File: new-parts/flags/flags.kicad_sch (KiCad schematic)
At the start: 12 parts, among them J1 BHR-10-VUA, J2 Conn_02x03_Odd_Even, K1 J104D2C12VDC.15S

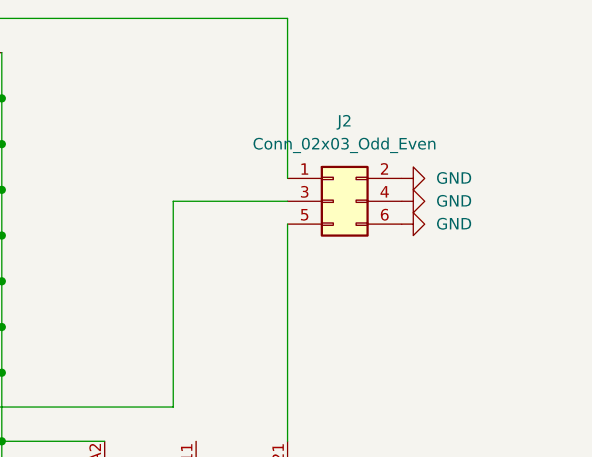
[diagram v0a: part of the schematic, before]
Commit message: Change all two-pin headers for control + ground to control only.
This is to prevent accidental short circuits when they are plugged in the
wrong way.
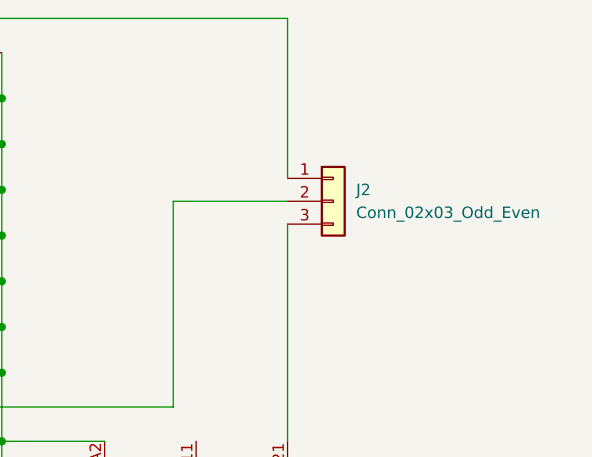
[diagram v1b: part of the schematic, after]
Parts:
- J2: footprint Connector_IDC:IDC-Header_2x03_P2.54mm_Vertical -> Connector_PinHeader_2.54mm:PinHeader_1x03_P2.54mm_Vertical; symbol Connector_Generic:Conn_02x03_Odd_Even -> Connector_Generic:Conn_01x03
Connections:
- net GND: no longer J2.2 (Pin_2), J2.4 (Pin_4), J2.6 (Pin_6)
- net at D8.2 (A), J1.8 (Pin_8): now also J2.2 (Pin_2); no longer J2.3 (Pin_3)
- net at K1.21: now also J2.3 (Pin_3); no longer J2.5 (Pin_5)
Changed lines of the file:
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@@
-    )
-  )
-  (symbol (lib_id "power:GND") (at 137.16 80.01 90) (unit 1)
-    (in_bom yes) (on_board yes) (dnp no) (fields_autoplaced)
-    (property "Reference" "#PWR09" (at 143.51 80.01 0)
-      (effects (font (size 1.27 1.27)) hide)
-    )
-    (property "Value" "GND" (at 140.97 80.01 90)
-      (effects (font (size 1.27 1.27)) (justify right))
-    )
-    (property "Footprint" "" (at 137.16 80.01 0)
-      (effects (font (size 1.27 1.27)) hide)
-    )
-    (property "Datasheet" "" (at 137.16 80.01 0)
-      (effects (font (size 1.27 1.27)) hide)
-    )
-    (pin "1")
-    (instances
-      (project "flags"
-        (path "/8e7358e7-c3ef-4f3e-9154-e7eba01c544e"
-          (reference "#PWR09") (unit 1)
-        )
-      )
     )
   )
@@
     )
   )
-  (symbol (lib_id "Connector_Generic:Conn_02x03_Odd_Even") (at 129.54 80.01 0) (unit 1)
-    (in_bom yes) (on_board yes) (dnp no) (fields_autoplaced)
-    (property "Reference" "J2" (at 130.81 71.12 0)
-      (effects (font (size 1.27 1.27)))
-    )
-    (property "Value" "Conn_02x03_Odd_Even" (at 130.81 73.66 0)
-      (effects (font (size 1.27 1.27)))
-    )
-    (property "Footprint" "Connector_IDC:IDC-Header_2x03_P2.54mm_Vertical" (at 129.54 80.01 0)
+  (symbol (lib_id "Connector_Generic:Conn_01x03") (at 129.54 80.01 0) (unit 1)
+    (in_bom yes) (on_board yes) (dnp no) (fields_autoplaced)
+    (property "Reference" "J2" (at 132.08 78.74 0)
+      (effects (font (size 1.27 1.27)) (justify left))
+    )
+    (property "Value" "Conn_02x03_Odd_Even" (at 132.08 81.28 0)
+      (effects (font (size 1.27 1.27)) (justify left))
+    )
+    (property "Footprint" "Connector_PinHeader_2.54mm:PinHeader_1x03_P2.54mm_Vertical" (at 129.54 80.01 0)
       (effects (font (size 1.27 1.27)) hide)
     )
@@
       (effects (font (size 1.27 1.27)) hide)
     )
-    (pin "5")
-    (pin "1")
-    (pin "6")
-    (pin "2")
-    (pin "4")
+    (pin "1")
+    (pin "2")
     (pin "3")
     (instances
@@
         (path "/8e7358e7-c3ef-4f3e-9154-e7eba01c544e"
           (reference "D3") (unit 1)
-        )
-      )
-    )
-  )
-  (symbol (lib_id "power:GND") (at 137.16 82.55 90) (unit 1)
-    (in_bom yes) (on_board yes) (dnp no) (fields_autoplaced)
-    (property "Reference" "#PWR010" (at 143.51 82.55 0)
-      (effects (font (size 1.27 1.27)) hide)
-    )
-    (property "Value" "GND" (at 140.97 82.55 90)
-      (effects (font (size 1.27 1.27)) (justify right))
-    )
-    (property "Footprint" "" (at 137.16 82.55 0)
-      (effects (font (size 1.27 1.27)) hide)
-    )
-    (property "Datasheet" "" (at 137.16 82.55 0)
-      (effects (font (size 1.27 1.27)) hide)
-    )
-    (pin "1")
-    (instances
-      (project "flags"
-        (path "/8e7358e7-c3ef-4f3e-9154-e7eba01c544e"
-          (reference "#PWR010") (unit 1)
         )
       )
@@
         )
       )
-    )
-  )
-  (symbol (lib_id "power:GND") (at 137.16 77.47 90) (unit 1)
-    (in_bom yes) (on_board yes) (dnp no) (fields_autoplaced)
-    (property "Reference" "#PWR08" (at 143.51 77.47 0)
-      (effects (font (size 1.27 1.27)) hide)
-    )
-    (property "Value" "GND" (at 140.97 77.47 90)
-      (effects (font (size 1.27 1.27)) (justify right))
-    )
-    (property "Footprint" "" (at 137.16 77.47 0)
-      (effects (font (size 1.27 1.27)) hide)
-    )
-    (property "Datasheet" "" (at 137.16 77.47 0)
-      (effects (font (size 1.27 1.27)) hide)
-    )
-    (pin "1")
-    (instances
-      (project "flags"
-        (path "/8e7358e7-c3ef-4f3e-9154-e7eba01c544e"
-          (reference "#PWR08") (unit 1)
-        )
-      )

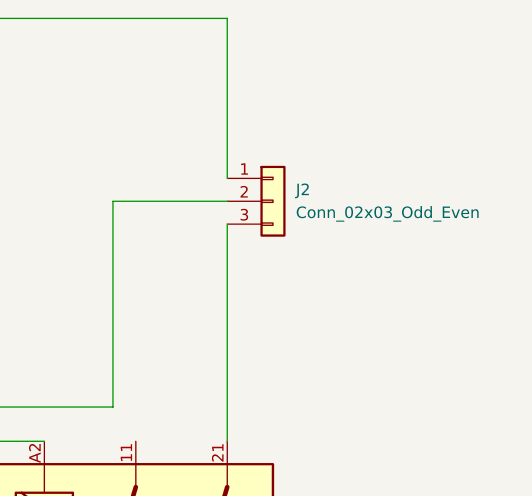
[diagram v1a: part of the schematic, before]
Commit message: Fix connector values: change names from 2 rows to 1 row.
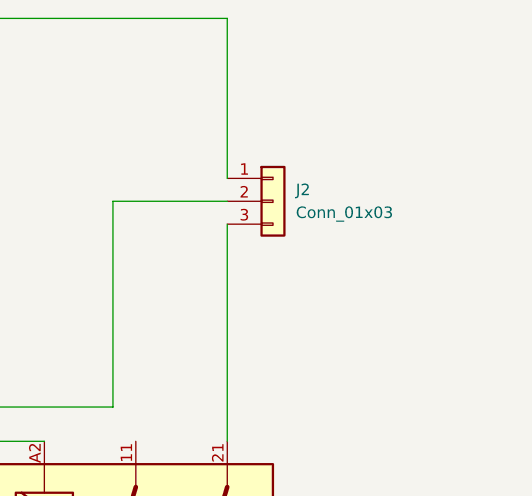
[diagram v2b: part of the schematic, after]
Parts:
- J2: value Conn_02x03_Odd_Even -> Conn_01x03
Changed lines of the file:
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@@
       (effects (font (size 1.27 1.27)) (justify left))
     )
-    (property "Value" "Conn_02x03_Odd_Even" (at 132.08 81.28 0)
+    (property "Value" "Conn_01x03" (at 132.08 81.28 0)
       (effects (font (size 1.27 1.27)) (justify left))
     )
